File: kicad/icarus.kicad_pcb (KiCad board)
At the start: 4 copper layers, 66.9 x 44.2 mm, 78 parts, among them J1 CAN Bus, J2 CAN Bus, J3 SWD Programming, J4 USB_B_Micro, U1 MAX15062A, U10 XT30, U11 XT30, U12 XT30, U13 LT1787HVIMS8PBF, U14 USBLC6-2SC6, U15 STLM20DD9FUDFN-4L_STM-L, U2 STM32G474CEU6, U3 TCAN334G, U4 XT90, U5 FSV10150VTO277-3L_ONS-L, U6 XT30, U7 XT30, U8 TPS2490DGSR, U9 XT30

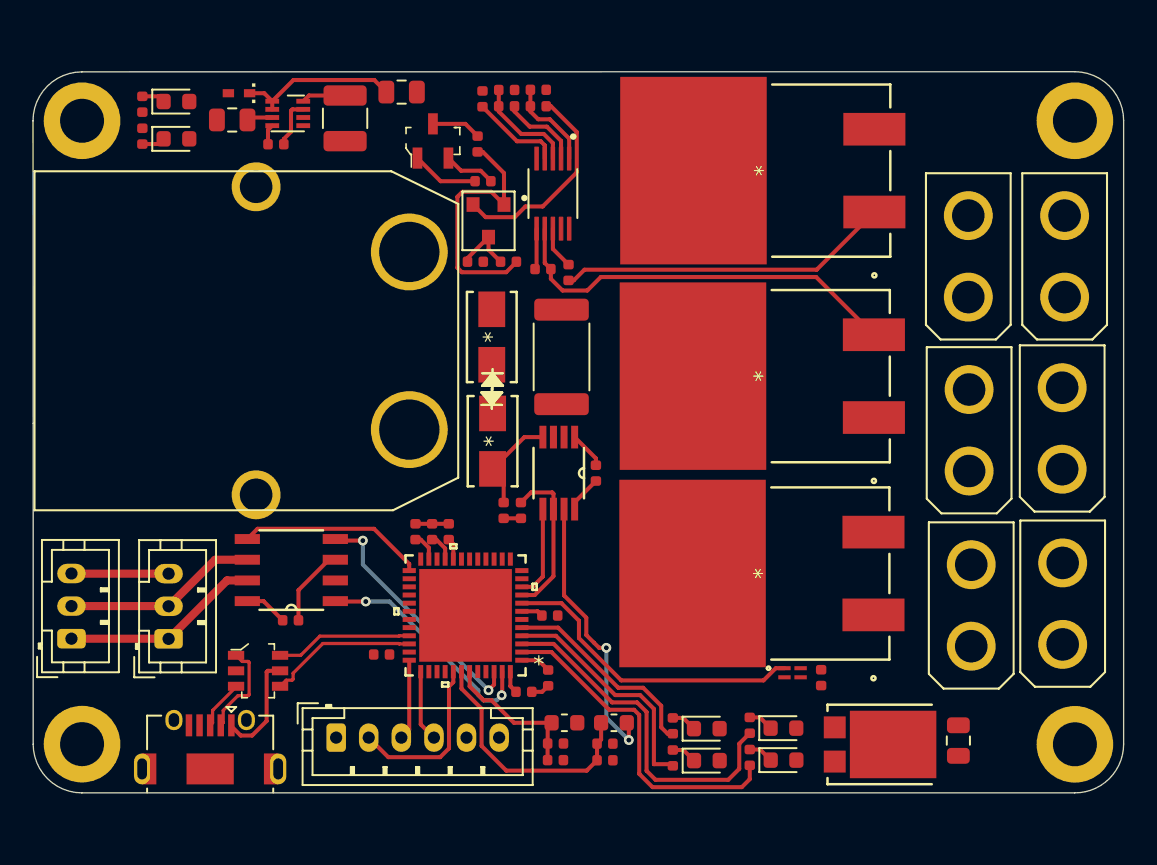
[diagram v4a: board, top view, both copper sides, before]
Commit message: Added ground plane, adjusted schematic
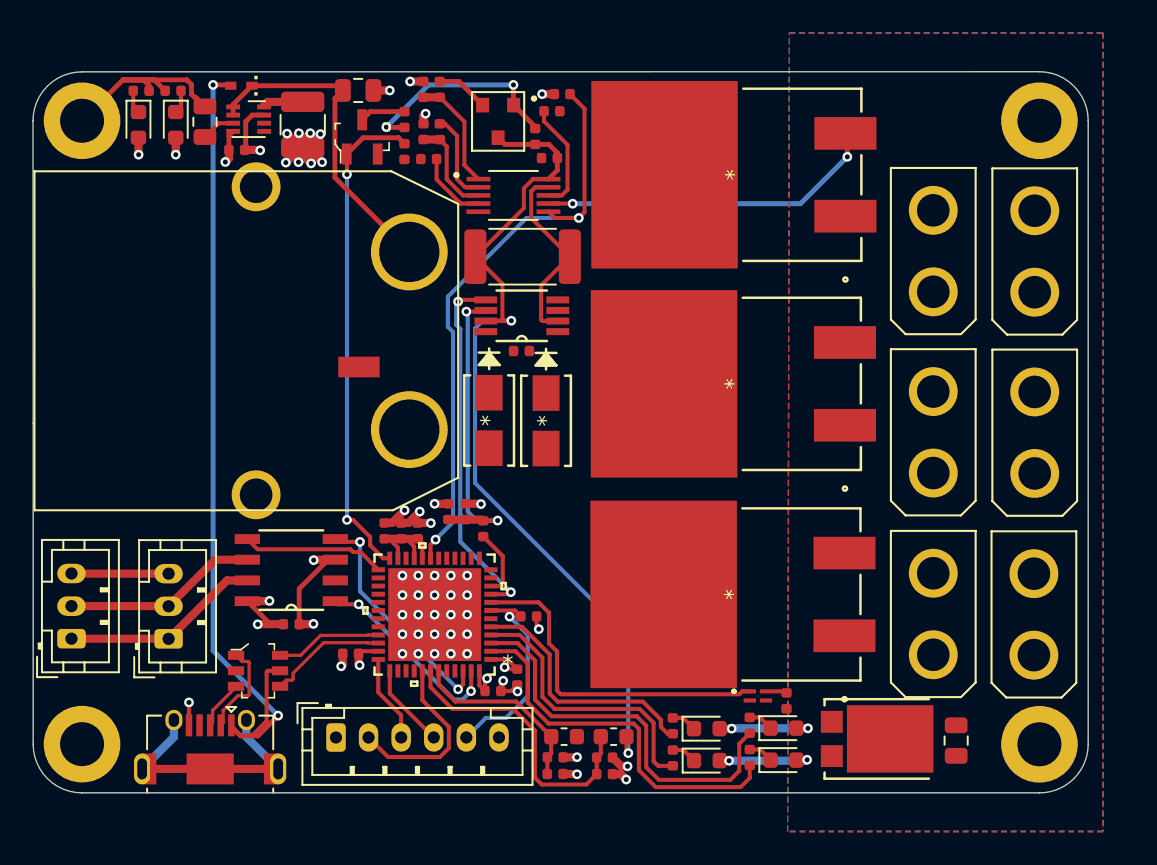
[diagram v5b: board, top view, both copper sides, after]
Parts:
- added JP1: Jumper_2_Bridged, icarus_kicad_lib:SHORT_TOP-BIG, F.Cu at (132.7, 98.3)
- added R18: 6.8k, 1%, Resistor_SMD:R_0402_1005Metric, F.Cu at (138.2, 107.2)
- R17: value R_Small -> 6.8k, 1%
- moved R15 10.8 mm to (145.2, 81.5), turned to 180 degrees
- moved R6 9.95 mm to (144.6, 82.6), turned to 0 degrees
- moved U13 9.92 mm to (142.7, 95.1), turned to 180 degrees
- moved C15 8.77 mm to (142.7, 97.3), turned to 0 degrees
- moved R2 7.86 mm to (143.5, 84.1), turned to 270 degrees
- moved C6 7.82 mm to (144.4, 85.5), turned to 180 degrees
- moved R9 7.06 mm to (136.7, 81.2), turned to 90 degrees
- moved R1 6.60 mm to (142.8, 91.5), turned to 180 degrees
- moved R7 6.13 mm to (137.7, 81.2), turned to 270 degrees
- moved MOSFET2 6.13 mm to (141.2, 83.2)
- moved CR1 6.12 mm to (144.2, 101.6), turned to 270 degrees
- moved R16 5.71 mm to (136.7, 83.8), turned to 90 degrees
- moved R8 5.15 mm to (135.5, 85.0), turned to 270 degrees
- moved C14 4.95 mm to (137.0, 85.5), turned to 0 degrees
- moved R3 4.73 mm to (135.5, 83.1)
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- renumbered R11 to R10, R12 to R11, R13 to R12, R14 to R13, R15 to R14, R2 to R15, R18 to R19, R3 to R2, R19 to R20, R20 to R21, R21 to R22, R4 to R3, R5 to R4, R6 to R5, R7 to R6, R8 to R7, R9 to R8, R10 to R9
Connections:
- C7 pad 2: GND -> GNDPWR
- CR1 pad 2: GND -> GNDPWR
- CR2 pad 2: GND -> GNDPWR
- R15 pad 2: OUT -> +3V3
- U10 pad -: GND -> GNDPWR
- U11 pad -: GND -> GNDPWR
- U12 pad -: GND -> GNDPWR
- U13 pad 6: I_SENSE_BIAS -> Net-(C16-Pad1)
- U2 pad 10: I_SENSE -> I_SENSE_BIAS
- U2 pad 19: Net-(U2-Pad19) -> PG
- U2 pad 24: Net-(U2-Pad24) -> TPS_ENABLE
- U2 pad 44: TPS_ENABLE -> Net-(U2-Pad44)
- U2 pad 9: I_SENSE_BIAS -> I_SENSE
- U4 pad -: GND -> Net-(U4-Pad-)
- U5 pad 1: GND -> GNDPWR
- U5 pad 2: GND -> GNDPWR
- U6 pad -: GND -> GNDPWR
- U7 pad -: GND -> GNDPWR
- U9 pad -: GND -> GNDPWR
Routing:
- net +5V: track 6.69 -> 51.8 mm, vias 0 -> 2
- net VSENSE_HIGH: track 31.0 -> 73.6 mm
- net +3V3: track 14.1 -> 48.8 mm, vias 0 -> 21
- net PG: track 2.52 -> 36.9 mm, vias 0 -> 2
- net TPS_ENABLE: track 4.12 -> 30.5 mm, vias 0 -> 2
- net GND: track 24.3 -> 49.5 mm, vias 0 -> 45
- net Net-(MOSFET1-Pad1): track 20.5 -> 0.00 mm
- net Net-(C16-Pad1): track 1.06 -> 18.7 mm, vias 0 -> 2
- net I_SENSE: track 5.69 -> 22.3 mm, vias 0 -> 2
- net Net-(J4-Pad6): track 0.00 -> 16.0 mm
- net VSENSE_LOW: track 0.00 -> 11.8 mm
- net NRST: track 1.44 -> 12.8 mm, vias 0 -> 1
- net Net-(MOSFET2-PadP$2): track 12.8 -> 3.23 mm
- net I_SENSE_BIAS: track 9.77 -> 4.21 mm
- net OUT: track 25.2 -> 21.0 mm, vias 0 -> 2
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- added copper zone on F.Cu, net GNDPWR
- added copper zone on B.Cu, net OUT
- added copper zone on In2.Cu-3V3, net OUT
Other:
- board size 66.9 x 44.2 mm -> 64.7 x 44.2 mm
- rule trace_min: 0.16 -> 0.15

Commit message: Layout v1.0 done
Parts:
- moved U13 8.70 mm to (142.8, 103.8)
- moved C15 8.70 mm to (142.8, 106.0)
- moved C7 7.64 mm to (161.9, 119.5)
- moved JP1 4.42 mm to (130.5, 102.1)
- moved CR1 3.80 mm to (144.2, 97.8)
- moved CR2 3.80 mm to (140.7, 97.8)
- moved U5 2.26 mm to (166.7, 121.5)
- moved R15 1.32 mm to (145.4, 82.8)
- moved R6 0.80 mm to (144.8, 81.8)
- moved MOSFET3 0.73 mm to (155.7, 87.2)
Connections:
- H2 pad 1: GND -> Net-(H2-Pad1)
- H3 pad 1: GND -> Net-(H3-Pad1)
- U4 pad -: Net-(U4-Pad-) -> GNDPWR
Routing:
- net Net-(MOSFET1-Pad1): track 0.00 -> 60.0 mm
- net VSENSE_HIGH: track 73.6 -> 113.1 mm
- net GND: track 49.5 -> 73.6 mm, vias 45 -> 41
- net OUT: track 21.0 -> 40.5 mm, vias 2 -> 4
- net I_SENSE: track 22.3 -> 12.7 mm, vias 2 -> 0
- net PG: track 36.9 -> 46.2 mm
- net VSENSE_LOW: track 11.8 -> 20.1 mm
- net GNDPWR: track 0.00 -> 7.57 mm, vias 0 -> 5
- net Net-(C16-Pad1): track 18.7 -> 12.2 mm, vias 2 -> 0
- net +3V3: track 48.8 -> 53.6 mm, vias 21 -> 23
- net +5V: track 51.8 -> 49.3 mm
- net Net-(C15-Pad2): track 0.00 -> 2.45 mm
- net Net-(C15-Pad1): track 0.00 -> 2.20 mm
- net GATE: track 6.72 -> 7.35 mm
- added copper zone on In2.Cu, net +3V3
- added copper zone on F.Cu, net GND
- added copper zone on In1.Cu, net GND
- added copper zone on B.Cu, net GNDPWR
- added copper zone on In1.Cu, net GNDPWR
- added copper zone on In2.Cu, net GNDPWR
- added copper zone on F.Cu, net OUT
- added copper zone on In1.Cu, net OUT
- added copper zone on B.Cu, net VSENSE_HIGH
- added copper zone on F.Cu, net VSENSE_HIGH
- added copper zone on In1.Cu, net VSENSE_HIGH
- added copper zone on In2.Cu, net VSENSE_HIGH
- added copper zone on F.Cu, net VSENSE_LOW
- added copper zone on In1.Cu, net VSENSE_LOW
- removed copper zone on In2.Cu-3V3, net +3V3
- removed copper zone on In1.Cu-GND, net GND
- removed copper zone on B.Cu, net OUT
- removed copper zone on In2.Cu-3V3, net OUT
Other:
- net class Default: clearance 0.2 -> 0.16
- rule trace_clearance: 0.2 -> 0.16

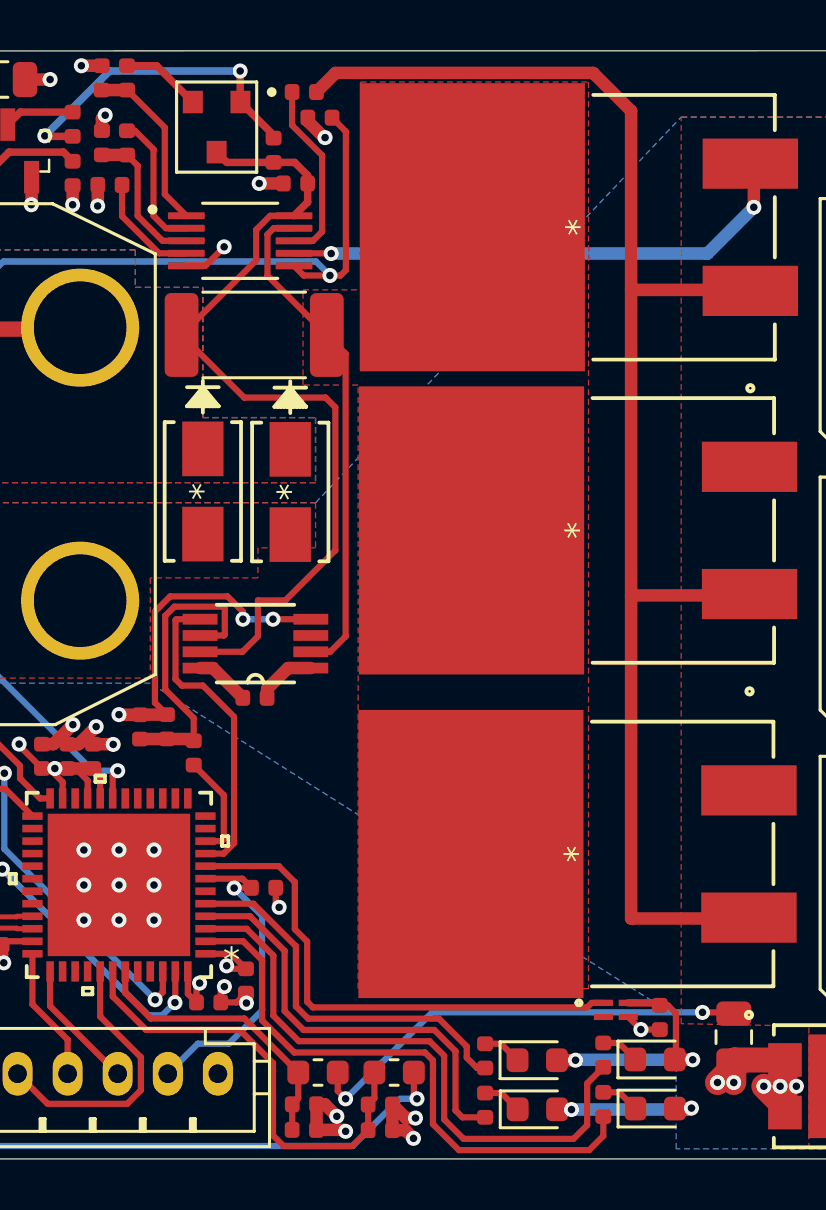
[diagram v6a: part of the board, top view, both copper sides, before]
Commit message: Updated BOM, updated layout to fix design rules
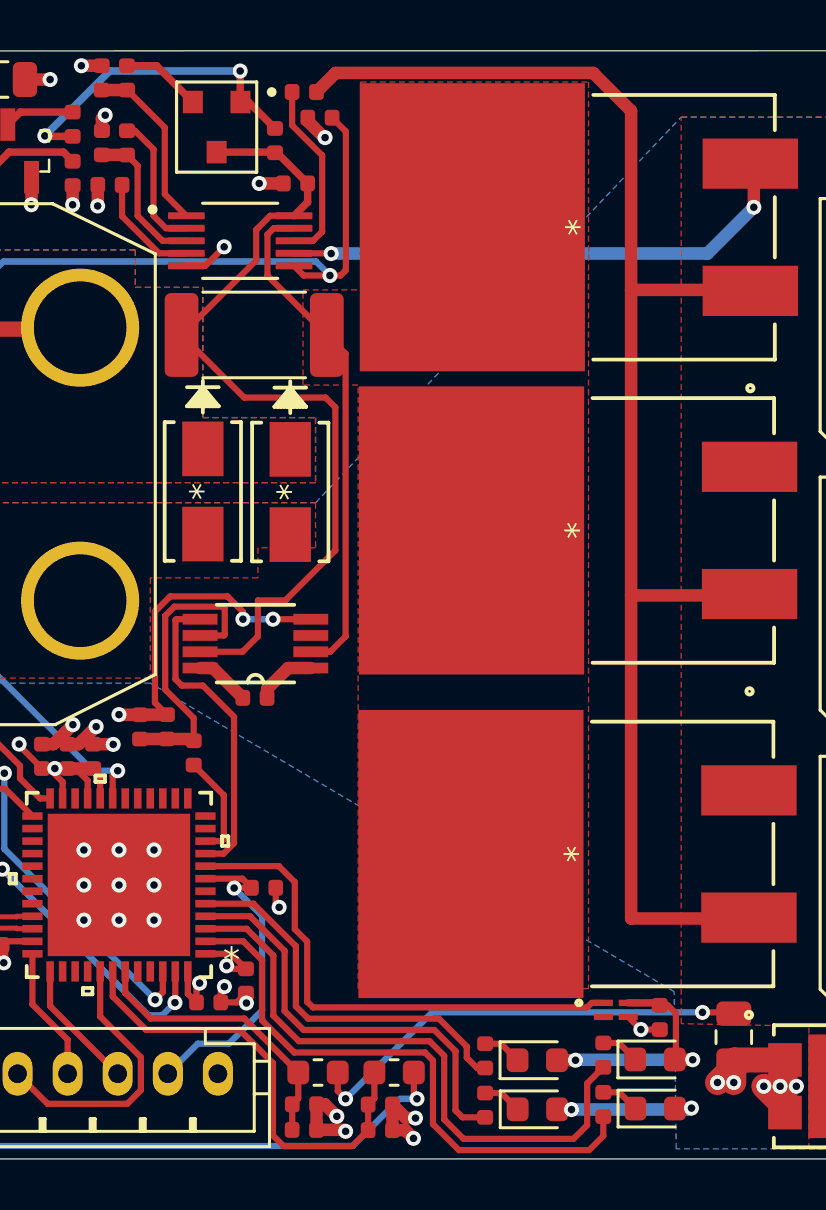
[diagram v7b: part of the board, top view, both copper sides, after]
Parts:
- moved R2 0.39 mm to (143.6, 83.7)
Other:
- rule trace_min: 0.15 -> 0.2

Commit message: Updated PCB layout
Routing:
- net GND: vias 41 -> 44
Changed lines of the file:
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@@
     (thickness 1.6)
     (drawings 11)
-    (tracks 599)
+    (tracks 602)
     (zones 0)
     (modules 80)
@@
   )
   (setup
-    (last_trace_width 0.3)
+    (last_trace_width 0.25)
     (user_trace_width 0.3)
     (user_trace_width 0.5)
@@
   (via (at 135.95 113.465) (size 0.6) (drill 0.3) (layers F.Cu B.Cu) (net 2))
   (via (at 137.35 113.465) (size 0.6) (drill 0.3) (layers F.Cu B.Cu) (net 2))
-  (via (at 135.95 114.865) (size 0.6) (drill 0.3) (layers F.Cu B.Cu) (net 2))
   (via (at 137.35 114.865) (size 0.6) (drill 0.3) (layers F.Cu B.Cu) (net 2))
   (via (at 138.75 114.865) (size 0.6) (drill 0.3) (layers F.Cu B.Cu) (net 2))
@@
   (segment (start 145.24 122.22) (end 145.24 123.235) (width 0.5) (layer F.Cu) (net 2))
   (segment (start 148.27 122.23) (end 148.27 123.25) (width 0.5) (layer F.Cu) (net 2))
+  (via (at 135.05 111.18) (size 0.6) (drill 0.3) (layers F.Cu B.Cu) (net 2))
+  (via (at 139.67 111.12) (size 0.6) (drill 0.3) (layers F.Cu B.Cu) (net 2))
+  (via (at 139.58 115.76) (size 0.6) (drill 0.3) (layers F.Cu B.Cu) (net 2))
+  (via (at 134.86 115.89) (size 0.6) (drill 0.3) (layers F.Cu B.Cu) (net 2))
   (segment (start 139.85 91.5) (end 142.82998 88.52002) (width 0.25) (layer F.Cu) (net 3))
   (segment (start 143.389456 86.74) (end 144.34 86.74) (width 0.25) (layer F.Cu) (net 3))
@@
   (segment (start 156.045848 118.349953) (end 156.225801 118.17) (width 0.25) (layer F.Cu) (net 47))
   (segment (start 145.092003 118.349953) (end 156.045848 118.349953) (width 0.25) (layer F.Cu) (net 47))
-  (segment (start 156.284199 81.036899) (end 157.8 82.5527) (width 0.5) (layer F.Cu) (net 63))
-  (segment (start 145.998101 81.036899) (end 156.284199 81.036899) (width 0.5) (layer F.Cu) (net 63))
-  (segment (start 145.235 81.8) (end 145.998101 81.036899) (width 0.5) (layer F.Cu) (net 63))
-  (segment (start 157.8 82.5527) (end 157.8 89.7) (width 0.5) (layer F.Cu) (net 63))
-  (segment (start 162.520399 89.7) (end 162.560399 89.74) (width 0.5) (layer F.Cu) (net 63))
-  (segment (start 157.8 89.7) (end 162.520399 89.7) (width 0.5) (layer F.Cu) (net 63))
-  (segment (start 157.8 89.7) (end 157.8 101.9) (width 0.5) (layer F.Cu) (net 63))
-  (segment (start 162.475399 101.9) (end 162.530399 101.845) (width 0.5) (layer F.Cu) (net 63))
-  (segment (start 157.8 101.9) (end 162.475399 101.9) (width 0.5) (layer F.Cu) (net 63))
-  (segment (start 157.8 101.9) (end 157.8 114.8) (width 0.5) (layer F.Cu) (net 63))
-  (segment (start 162.470001 114.8) (end 162.505001 114.765) (width 0.5) (layer F.Cu) (net 63))
-  (segment (start 157.8 114.8) (end 162.470001 114.8) (width 0.5) (layer F.Cu) (net 63))
+  (segment (start 158.105 114.765) (end 162.505001 114.765) (width 0.25) (layer F.Cu) (net 63))
+  (segment (start 158.1 114.76) (end 158.105 114.765) (width 0.25) (layer F.Cu) (net 63))
+  (segment (start 157.2 80.66) (end 158.1 81.56) (width 0.25) (layer F.Cu) (net 63))
+  (segment (start 146.375 80.66) (end 157.2 80.66) (width 0.25) (layer F.Cu) (net 63))
+  (segment (start 145.235 81.8) (end 146.375 80.66) (width 0.25) (layer F.Cu) (net 63))
+  (segment (start 158.105 101.845) (end 158.1 101.85) (width 0.25) (layer F.Cu) (net 63))
+  (segment (start 162.530399 101.845) (end 158.105 101.845) (width 0.25) (layer F.Cu) (net 63))
+  (segment (start 158.1 101.85) (end 158.1 114.76) (width 0.25) (layer F.Cu) (net 63))
+  (segment (start 158.11 89.74) (end 158.1 89.73) (width 0.25) (layer F.Cu) (net 63))
+  (segment (start 162.560399 89.74) (end 158.11 89.74) (width 0.25) (layer F.Cu) (net 63))
+  (segment (start 158.1 89.73) (end 158.1 101.85) (width 0.25) (layer F.Cu) (net 63))
+  (segment (start 158.1 81.56) (end 158.1 89.73) (width 0.25) (layer F.Cu) (net 63))
   (segment (start 121.79 82.305) (end 121.47 82.625) (width 0.25) (layer F.Cu) (net 64))
   (segment (start 121.79 81.32) (end 121.79 82.305) (width 0.25) (layer F.Cu) (net 64))
